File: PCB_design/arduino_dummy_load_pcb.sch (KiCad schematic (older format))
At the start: 75 parts

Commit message: Created protection circuitry for channel B, added decoupling capacitor for 78L05, rearranged a few elements
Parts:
- added C?: C, symbol C
- added D? (x3): D, symbol D
- added R?: 10k, symbol R
- added R? (x2): 4.7k, symbol R
- added RV? (x2): POT, symbol POT
- added T? (x2): TMP36, symbol TMP36
- added U? (x2): LM324, symbol LM324
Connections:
- wire segments 162 -> 190
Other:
- moved on the sheet: D?, J?, Q?, R?, RSA1, RSA2, RSA3, RV?, U?A

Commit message: Added lithium ion charging circuitry and labeled all components
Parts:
- removed C?: CP1, symbol CP1
- removed D? (x2): D, symbol D
- removed Q? (x2): IRF540N, TO_SOT_Packages_THT:TO-220_Vertical, symbol IRF540N
- removed R? (x20): 10, symbol R
- removed R? (x2): 10k, symbol R
- removed R? (x2): 1k, symbol R
- removed RV?: POT, symbol POT
- removed U? (x6): LM324, symbol LM324
- removed U?: L78L05_TO92, TO_SOT_Packages_THT:TO-92_Inline_Narrow_Oval, symbol L78L05_TO92
- added CA1, CB1: 10uF, symbol C
- added CA2, CA3, CB2, CB3: 100nF, symbol C
- added DB4, DB5: D, symbol D
- added M1: REG, symbol REG
- added QA3, QB3: IRF9540N, TO_SOT_Packages_THT:TO-220_Vertical, symbol IRF9540N
- added QB1, QB2: IRF540N, TO_SOT_Packages_THT:TO-220_Vertical, symbol IRF540N
- added RA6, RB2, RB4, RB6: 10k, symbol R
- added RA7, RB7: 4.7k, symbol R
- added RB3, RB5: 1k, symbol R
- added RSB1, RSB10, RSB11, RSB12, RSB13, RSB14, RSB15, RSB16, RSB17, RSB18, RSB19, RSB2, RSB20, RSB3, RSB4, RSB5, RSB6, RSB7, RSB8, RSB9: 10, symbol R
- added RVA1: POT, symbol POT
- added unit 2 of U1
- added unit 3 of U1
- added unit 4 of U1
- added unit 4 of U2
- added unit 3 of U2
- added unit 2 of U2
- added UA2, UB2: MCP73826, symbol MCP73826
- C1: renamed from C?; value C -> 10uF
- gave numbers to parts that had none: 47
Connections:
- net labels added: CHARGE
- wire segments 190 -> 224
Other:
- moved on the sheet: C1, DA1, DA2, DA3, DA4, DB1, DB2, DB3, J1, QA2, R1, R2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

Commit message: Fixed connector. This should be the first version of the schematic which is fully functional, but completly untested.
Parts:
- removed J2: Conn_01x04, symbol Conn_01x04
- added J2: Conn_02x08_Counter_Clockwise, symbol Conn_02x08_Counter_Clockwise
- added R3, R4, R5, R6, R7: 4.7k, symbol R
- RA6, RB6: value 10k -> 0.1
- renumbered R3 to R8
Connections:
- net labels added: Iout_A
- wire segments 224 -> 245
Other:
- moved on the sheet: C1, CA1, CA2, CA3, CB1, CB2, CB3, DA1, DA2, DA3, DB1, DB2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

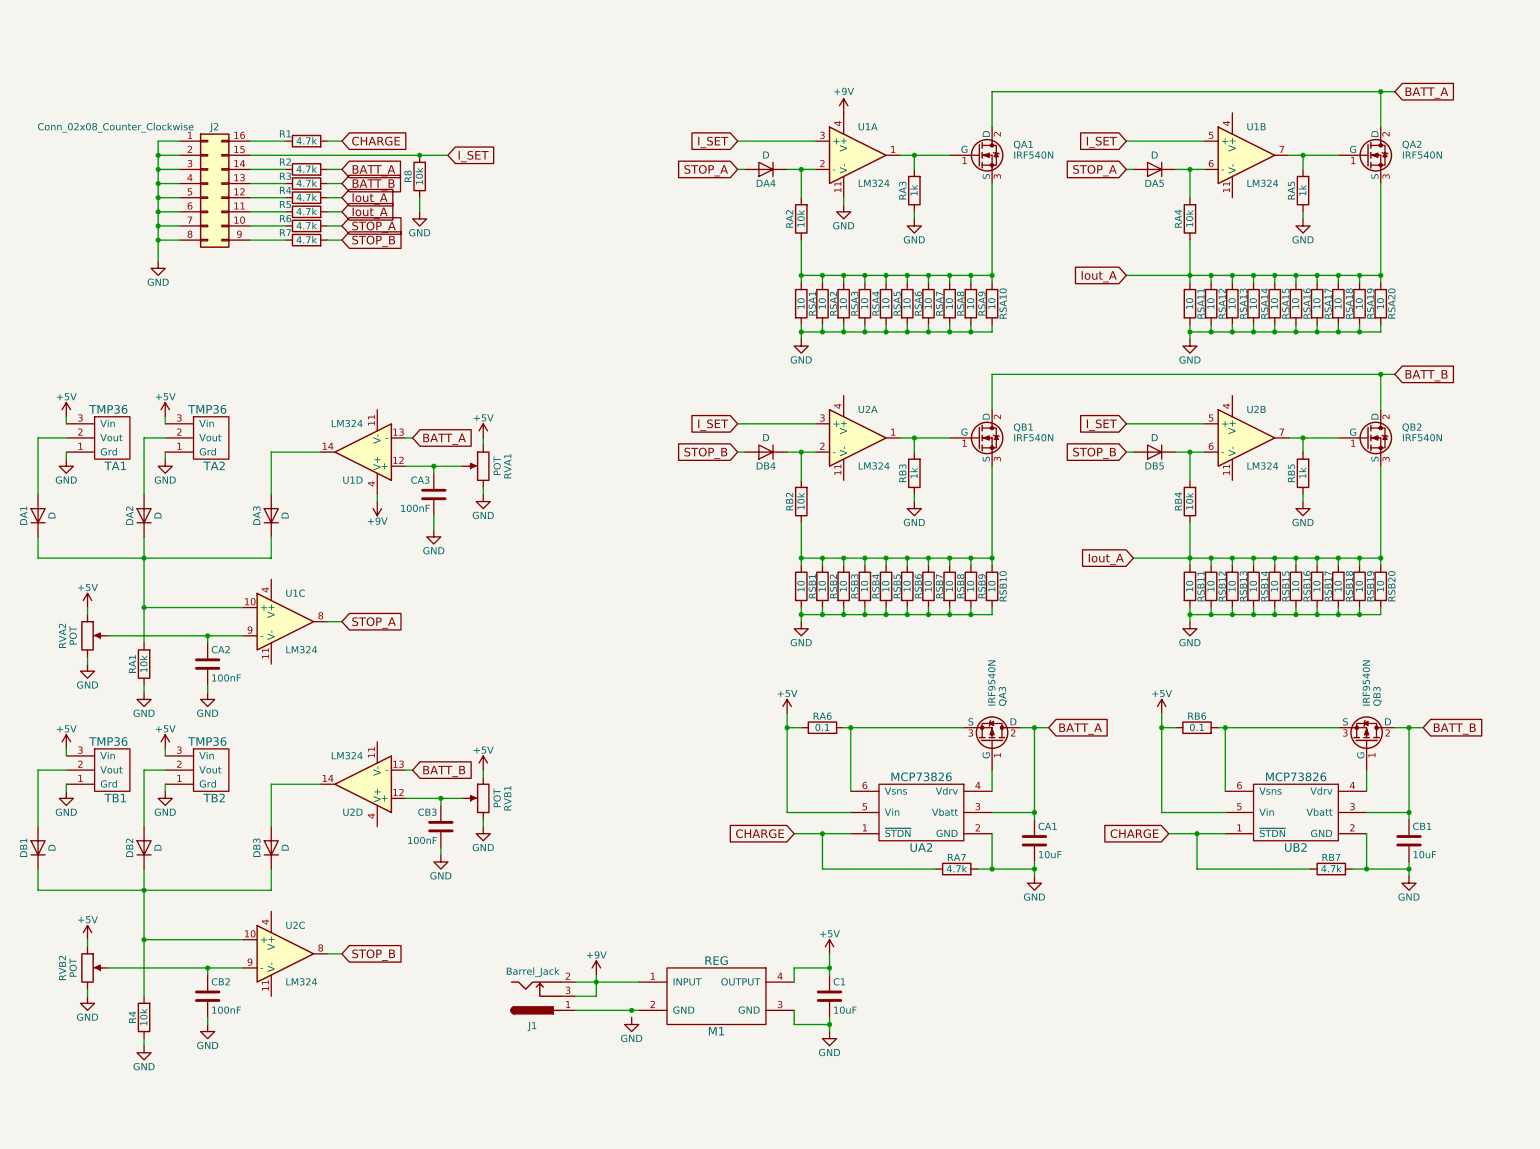
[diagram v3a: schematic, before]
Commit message: Fixed a few "bugs" (forgot to do DRC check!) and also added the batteries!
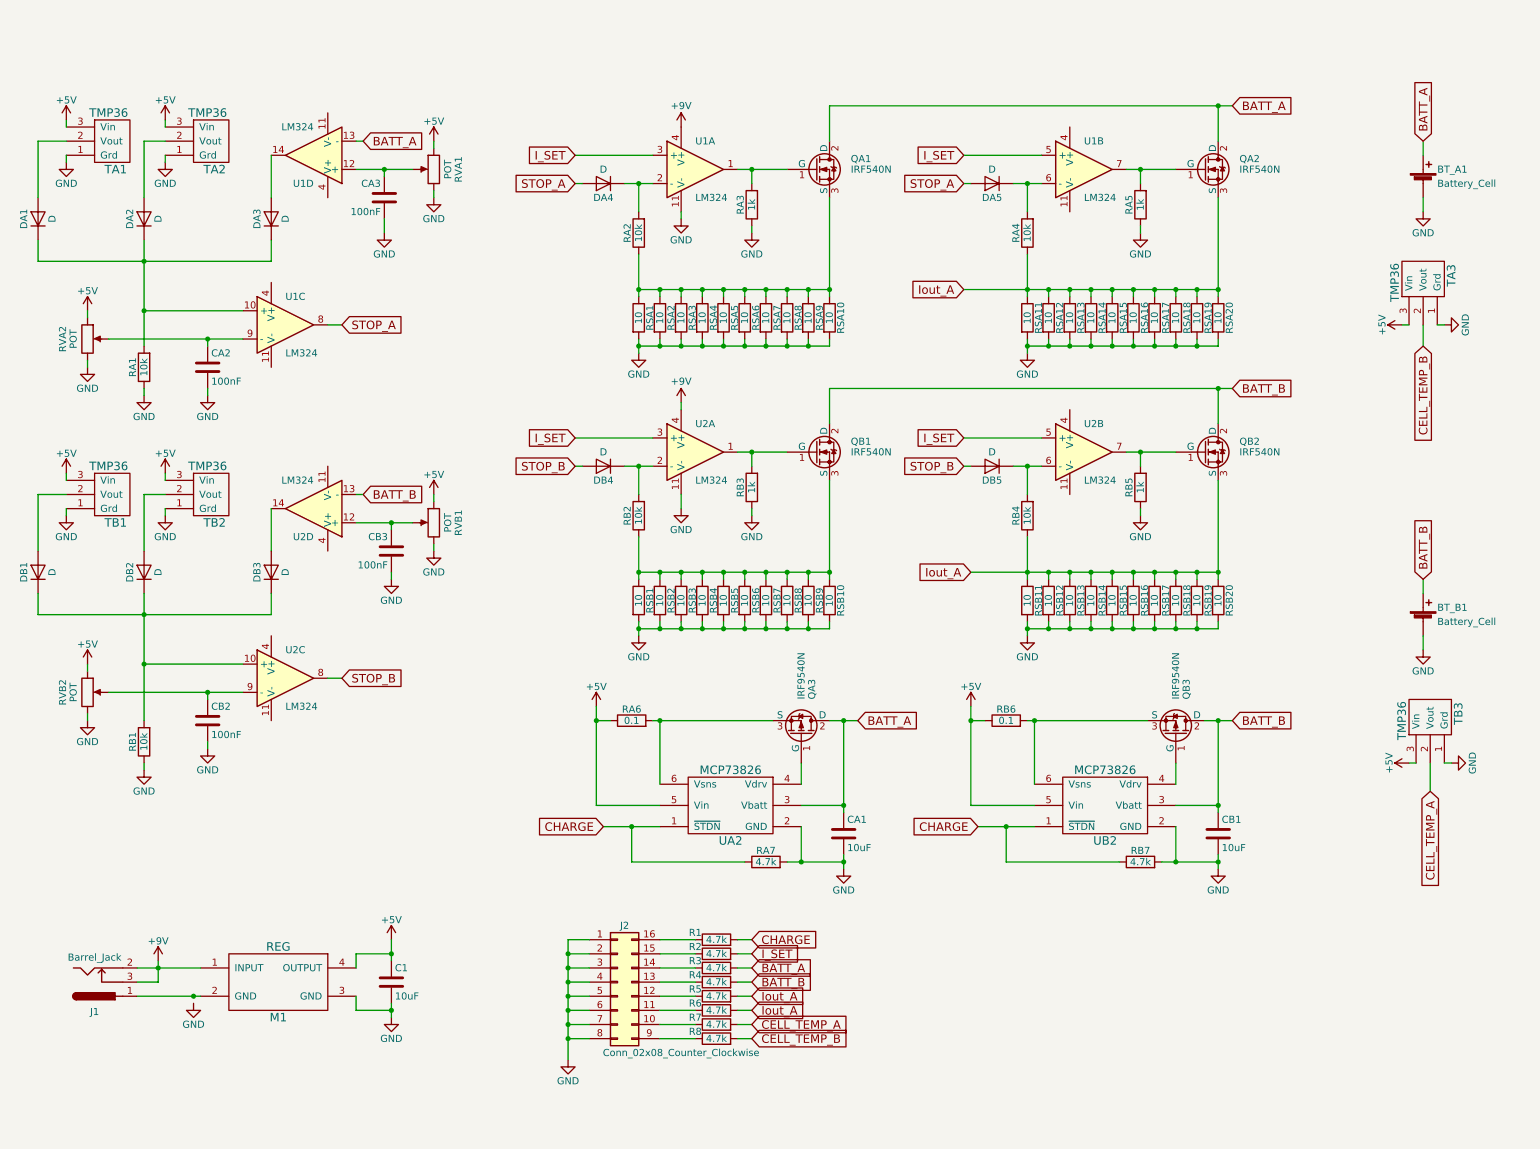
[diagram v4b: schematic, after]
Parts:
- added BT_A1, BT_B1: Battery_Cell, symbol Battery_Cell
- added TA3, TB3: TMP36, symbol TMP36
- R8: value 10k -> 4.7k
- renumbered R4 to RB1
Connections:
- net +5V: now also TA3.3 (Vin), TB3.3 (Vin)
- net +9V: now also U2.4 (V+); no longer U1.4 (V+)
- net BATT_A: now also R3.2, BT_A1.1 (+); no longer R2.2
- net BATT_B: now also R4.2, BT_B1.1 (+); no longer R3.2
- net GND: now also U2.11 (V-), BT_A1.2 (-), BT_B1.2 (-), TA3.1 (Grd), TB3.1 (Grd); no longer R8.1
- net I_SET: now also R2.2; no longer J2.15 (Pin_15), R8.2
- net Iout_A: now also R6.2; no longer R4.2
- net STOP_A: no longer R6.2
- net STOP_B: no longer R7.2
- net at R2.1: now also J2.15 (Pin_15); no longer J2.14 (Pin_14)
- net at J2.10 (Pin_10): now also R7.1; no longer R6.1
- net at J2.11 (Pin_11): now also R6.1; no longer R5.1
- net at J2.12 (Pin_12): now also R5.1; no longer R4.1
- net at J2.13 (Pin_13): now also R4.1; no longer R3.1
- net at J2.9 (Pin_9): now also R8.1; no longer R7.1
- new net: J2.14 (Pin_14), R3.1
- new net CELL_TEMP_A: R7.2, TB3.2 (Vout)
- new net CELL_TEMP_B: R8.2, TA3.2 (Vout)
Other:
- moved on the sheet: C1, CA1, CA2, CA3, CB1, CB2, CB3, DA1, DA2, DA3, DA4, DA5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

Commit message: Gave components footprints and started PCB layout
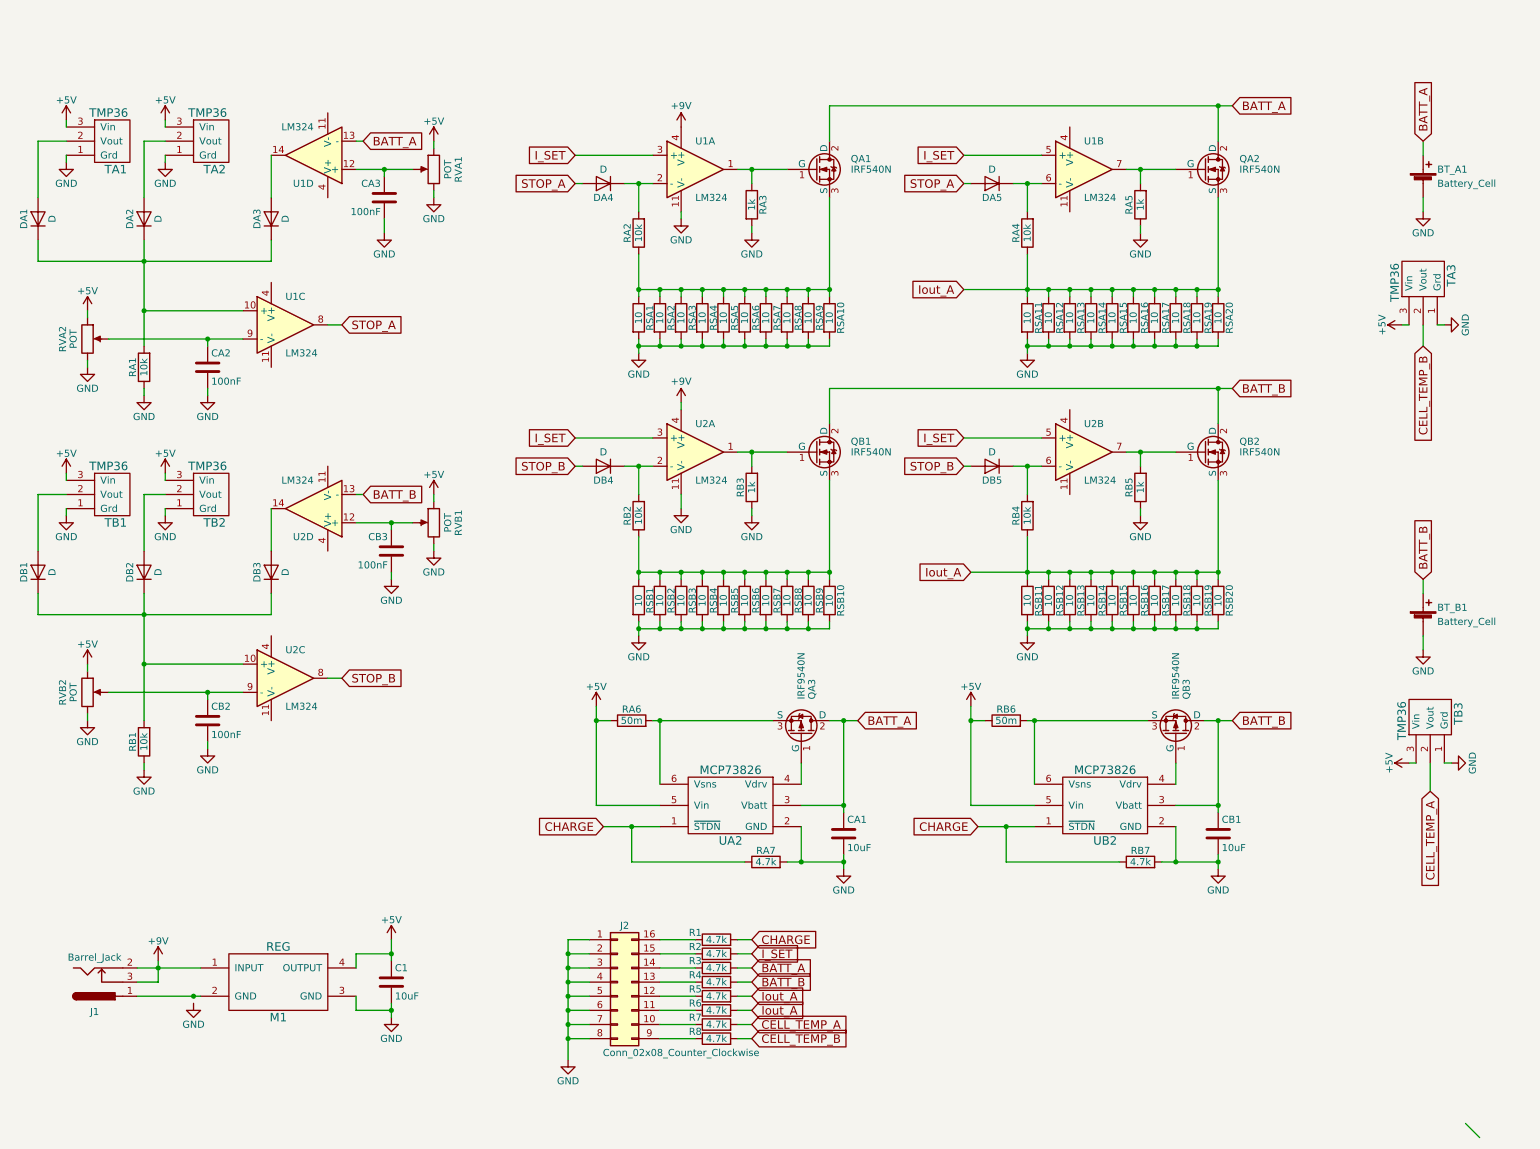
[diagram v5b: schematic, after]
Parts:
- C1, CA1, CA2, CA3, CB1, CB2, CB3: footprint (none) -> Capacitors_SMD:C_0805_HandSoldering
- DA1, DA2, DA3, DA4, DA5, DB1, DB2, DB3, DB4, DB5: footprint (none) -> Diodes_SMD:D_SOD-123
- R1, R2, R3, R4, R5, R6, R7, R8, RA1, RA2, RA3, RA4, RA5, RA7, RB1, RB7: footprint (none) -> Resistors_SMD:R_0805_HandSoldering
- RA6, RB6: value 0.1 -> 50m; footprint (none) -> Resistors_SMD:R_2512_HandSoldering
- RSA1, RSA10, RSA11, RSA12, RSA13, RSA14, RSA15, RSA16, RSA17, RSA18, RSA19, RSA2, RSA20, RSA3, RSA4, RSA5, RSA6, RSA7, RSA8, RSA9, RSB1, RSB10, RSB11, RSB12, RSB13, RSB14, RSB15, RSB16, RSB17, RSB18, RSB19, RSB2, RSB20, RSB3, RSB4, RSB5, RSB6, RSB7, RSB8, RSB9: footprint (none) -> Resistors_THT:R_Axial_DIN0617_L17.0mm_D6.0mm_P7.62mm_Vertical
- RVA1, RVA2, RVB1, RVB2: footprint (none) -> Potentiometers:Potentiometer_Trimmer_ACP_CA6v_Horizontal_MountLS
- TA1, TA2, TA3, TB1, TB2, TB3: footprint (none) -> TO_SOT_Packages_THT:TO-92_Inline_Wide
- U1, U2: footprint (none) -> Housings_SOIC:SOIC-14_3.9x8.7mm_Pitch1.27mm
- UA2, UB2: footprint (none) -> TO_SOT_Packages_SMD:SOT-23-6_Handsoldering
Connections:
- net GND: now also RA3.2; no longer RA3.1
- net at QA1.1 (G), U1.1: now also RA3.1; no longer RA3.2

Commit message: Latest commit
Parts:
- removed J2: Conn_02x08_Counter_Clockwise, symbol Conn_02x08_Counter_Clockwise
- added C2: 10uF, Capacitors_SMD:C_0805_HandSoldering, symbol C
- added CB?: 100nF, Capacitors_SMD:C_0805_HandSoldering, symbol C
- added J2: Conn_02x08_Odd_Even, symbol Conn_02x08_Odd_Even
- added R10, R9: 47k, Resistors_SMD:R_0805_HandSoldering, symbol R
- added U?: MCP3208, symbol MCP3208
- J1: footprint (none) -> Connectors:JACK_ALIM
- QA1, QA2, QA3, QB1, QB2, QB3: footprint TO_SOT_Packages_THT:TO-220_Vertical -> TO_SOT_Packages_THT:TO-220-3_Vertical
- R1, R2, R3, R4, R5, R6, R7, R8, RA7, RB7: value 4.7k -> 47k
- RA2, RA4, RB1: value 10k -> 47k
- RA3, RA5: value 1k -> 47k
- RB2, RB4: value 10k -> 47k; footprint (none) -> Resistors_SMD:R_0805_HandSoldering
- RB3, RB5: value 1k -> 47k; footprint (none) -> Resistors_SMD:R_0805_HandSoldering
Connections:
- net +5V: now also C2.1, CB?.1, U?.16 (Vdd)
- net BATT_B: now also R5.2; no longer R4.2
- net CELL_TEMP_A: now also R9.2; no longer R7.2
- net CELL_TEMP_B: now also R10.2; no longer R8.2
- net GND: now also R4.2, R6.2, C2.2, CB?.2, J2.1 (Pin_1), J2.11 (Pin_11), J2.13 (Pin_13), J2.15 (Pin_15), J2.3 (Pin_3), J2.5 (Pin_5), J2.7 (Pin_7), J2.9 (Pin_9), U?.14 (AGND), U?.9 (DGND); no longer M1.3 (GND)
- net Iout_A: now also R7.2, R8.2; no longer R5.2, R6.2
- net at R1.1: now also J2.2 (Pin_2)
- net at R2.1: now also J2.4 (Pin_4)
- net at R7.1: now also U?.3 (CH2)
- net at R6.1: now also R5.1, U?.2 (CH1)
- net at R4.1: now also R3.1, U?.1 (CH0)
- net at R8.1: now also U?.4 (CH3)
- new net: J2.12 (Pin_12), U?.10 (~CS~/SHDN)
- new net: J2.10 (Pin_10), U?.11 (Din)
- new net: J2.8 (Pin_8), U?.12 (Dout)
- new net: J2.6 (Pin_6), U?.13 (CLK)
- new net: R9.1, U?.5 (CH4)
- new net: R10.1, U?.6 (CH5)
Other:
- moved on the sheet: C1, J1, M1, R1, R2, R3, R4, R5, R6, R7, R8
